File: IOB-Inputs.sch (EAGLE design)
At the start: 20 parts, among them J1 RJ12/6

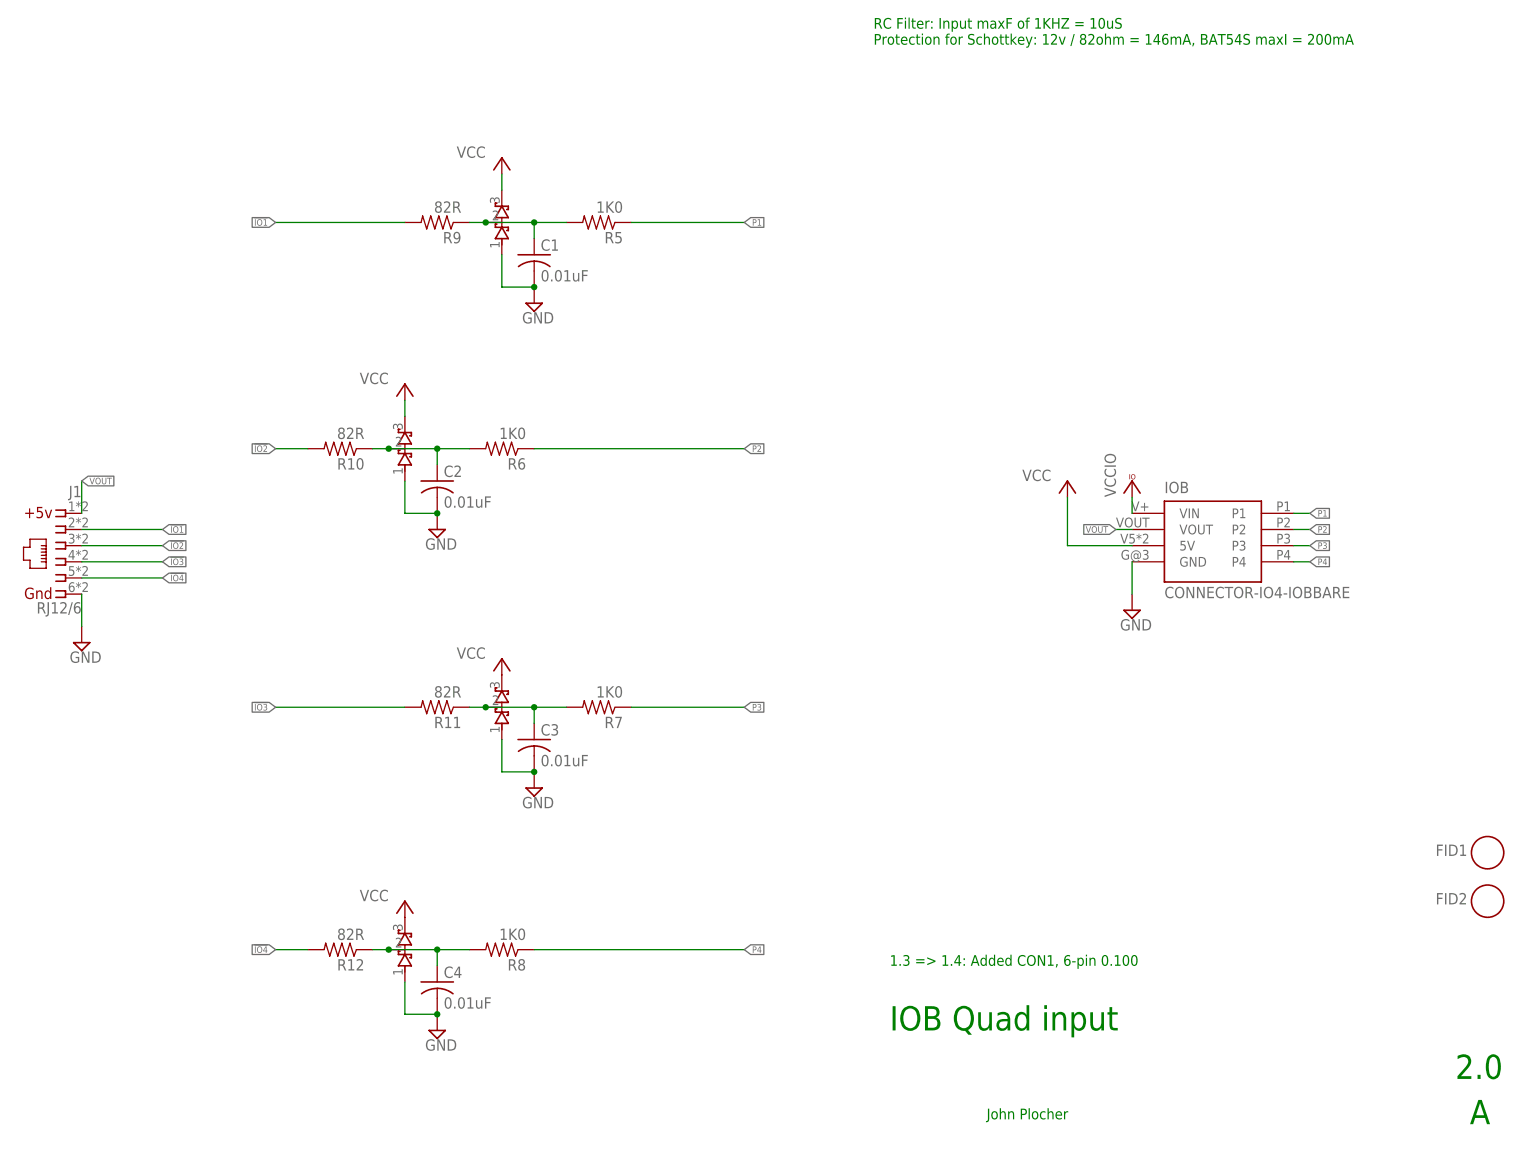
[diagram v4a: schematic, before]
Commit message: Replaced too small BAT54S SOT23R footprint with SOT23
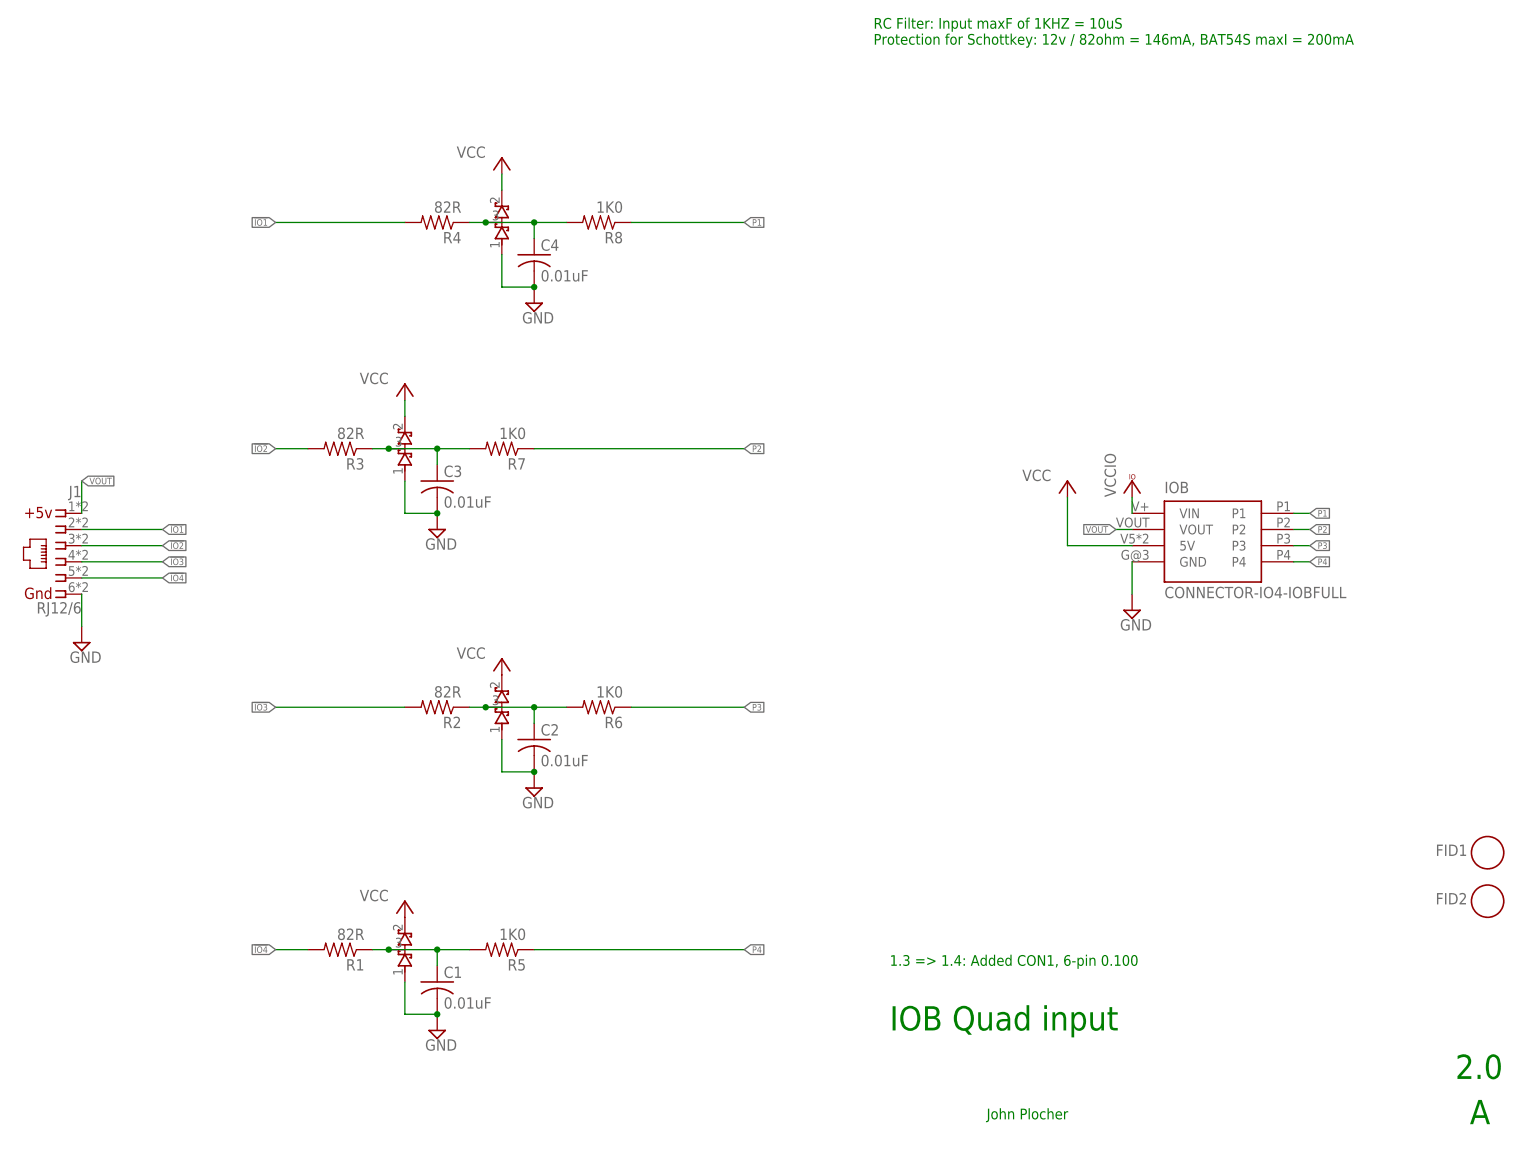
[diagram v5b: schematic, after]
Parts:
- D1, D2, D3, D4: value (none) -> BAT54S; device SPCoast:DIODE-BAT54S323R -> SPCoast:DIODE-BAT54S23
- IOB: value CONNECTOR-IO4-IOBBARE -> CONNECTOR-IO4-IOBFULL; device SPCoast:CONNECTOR-IO4-IOBBARE -> SPCoast:CONNECTOR-IO4-IOBFULL
- R5, R6, R7, R8: device SPCoast:R0805-RES -> SPCoast:R0603-RES
- renumbered R10 to R3, R11 to R2, R12 to R1, R9 to R4
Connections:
- net N$10: now also C1.1, D1.COM, R5.2; no longer C4.1, D4.COM, R8.2
- net N$12: now also C2.1, D2.COM, R6.2; no longer C3.1, D3.COM, R7.2
- net N$13: now also C3.1, D3.COM, R7.2; no longer C2.1, D2.COM, R6.2
- net N$14: now also C4.1, D4.COM, R8.2; no longer C1.1, D1.COM, R5.2
- net P1: now also R8.1; no longer R5.1
- net P2: now also R7.1; no longer R6.1
- net P3: now also R6.1; no longer R7.1
- net P4: now also R5.1; no longer R8.1
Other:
- moved on the sheet: C1, C2, C3, C4, R5, R6, R7, R8

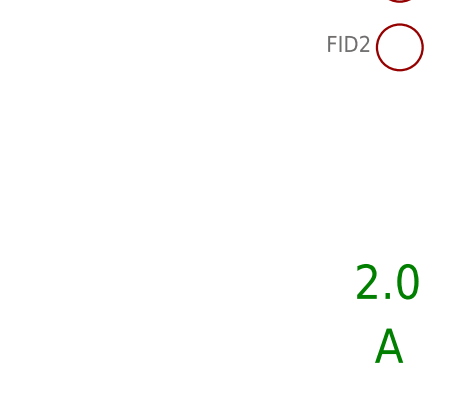
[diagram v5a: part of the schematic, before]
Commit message: Rev to 2.1 because of Stencil change
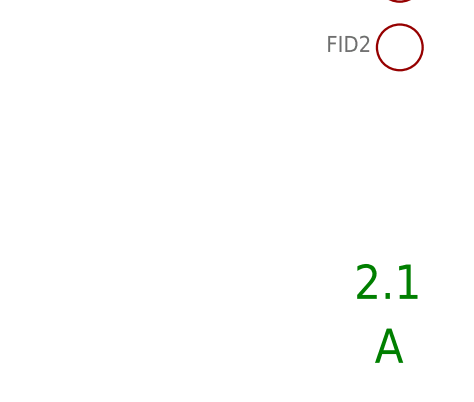
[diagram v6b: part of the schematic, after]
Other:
- note added: "2.1"
- note removed: "2.0"
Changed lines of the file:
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@@
 <plain>
 <text x="149.86" y="20.32" size="3.81" layer="91">IOB Quad input</text>
-<text x="238.76" y="12.7" size="3.81" layer="91">2.0</text>
+<text x="238.76" y="12.7" size="3.81" layer="91">2.1</text>
 <text x="241.046" y="5.588" size="3.81" layer="91">A</text>
 <text x="147.32" y="175.26" size="1.6764" layer="91">RC Filter: Input maxF of 1KHZ = 10uS
